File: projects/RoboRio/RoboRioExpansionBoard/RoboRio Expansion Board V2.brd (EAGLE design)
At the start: 56.6 x 77.5 mm, 125 parts, among them J1 RRINTERFACE-FEMALE, J10 SPI_MISO, J11 SPI_MOSI, J12 I2C_SCL, J13 I2C_SDA, J14 UART_TX, J15 UART_RX, J16 LCD, J17 ADC1, J18 ADC2, J19 ADC3, J2 MICROSD-HINGED, J20 ADC4, J21 ADC5, J22 ADC6, J23 ADC7, J25 PWM0, J26 PWM1, J27 PWM2, J28 PWM3, J29 PWM4, J3 51387-0578, J30 PWM5, J31 PWM6, J32 PWM7, J33 PWM8, J34 PWM9, J35 AI0, J36 AI1, J37 AI2, J38 AI3, J39 AO0, J4 GPIO0, J40 AO1, J5 GPIO1, J6 GPIO2, J7 GPIO3, J8 SPI_CS, J9 SPI_CLK, Q1 NPN-SOT416, Q2 NPN-SOT416, Q3 NPN-SOT416, U1 P8X32A-Q44_P, U2 24LC256ST, U3 FT232RL, U4 TC54VN43, U5 TPS2115APWR, U6 REG1117, U7 ADC124S01, U8 ADC124S01, Y1 5MHz

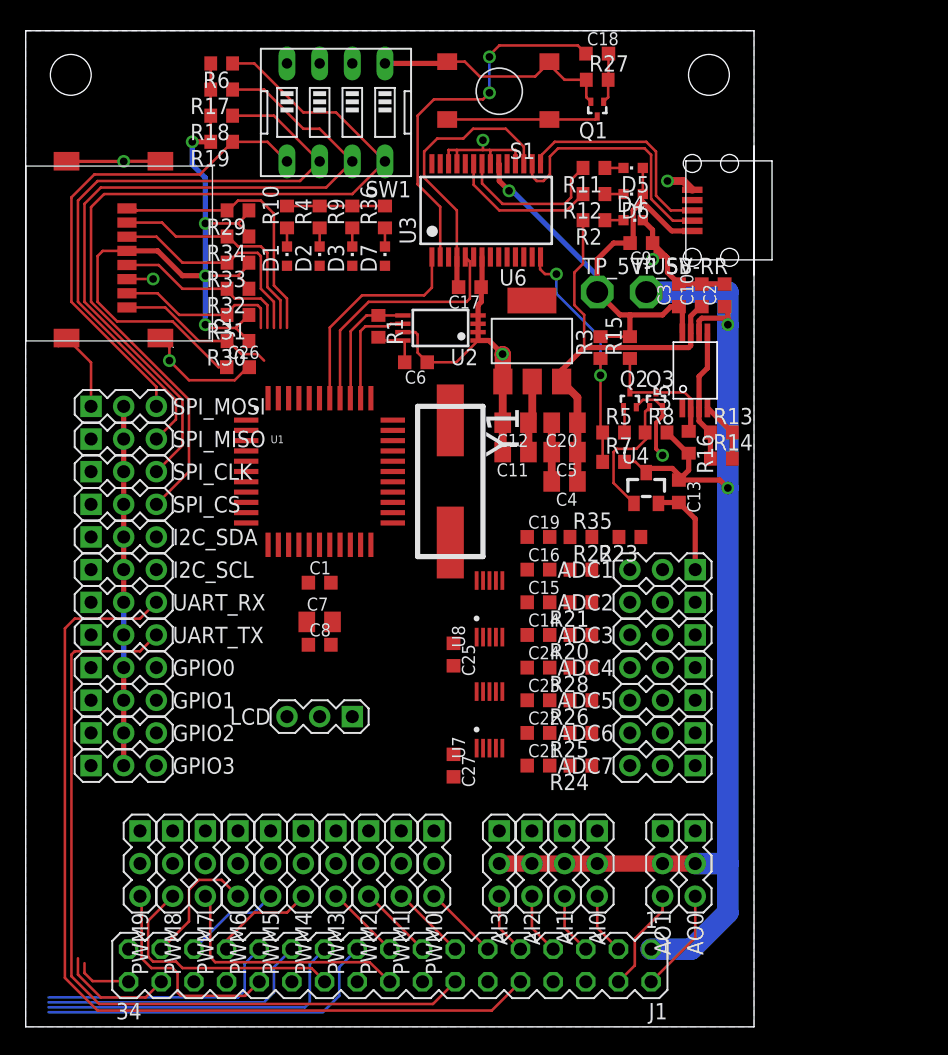
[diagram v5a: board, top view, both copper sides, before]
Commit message: Fixed ADC GND/DGND & VA/+3V3 issue
also lost of routing for the ADCs
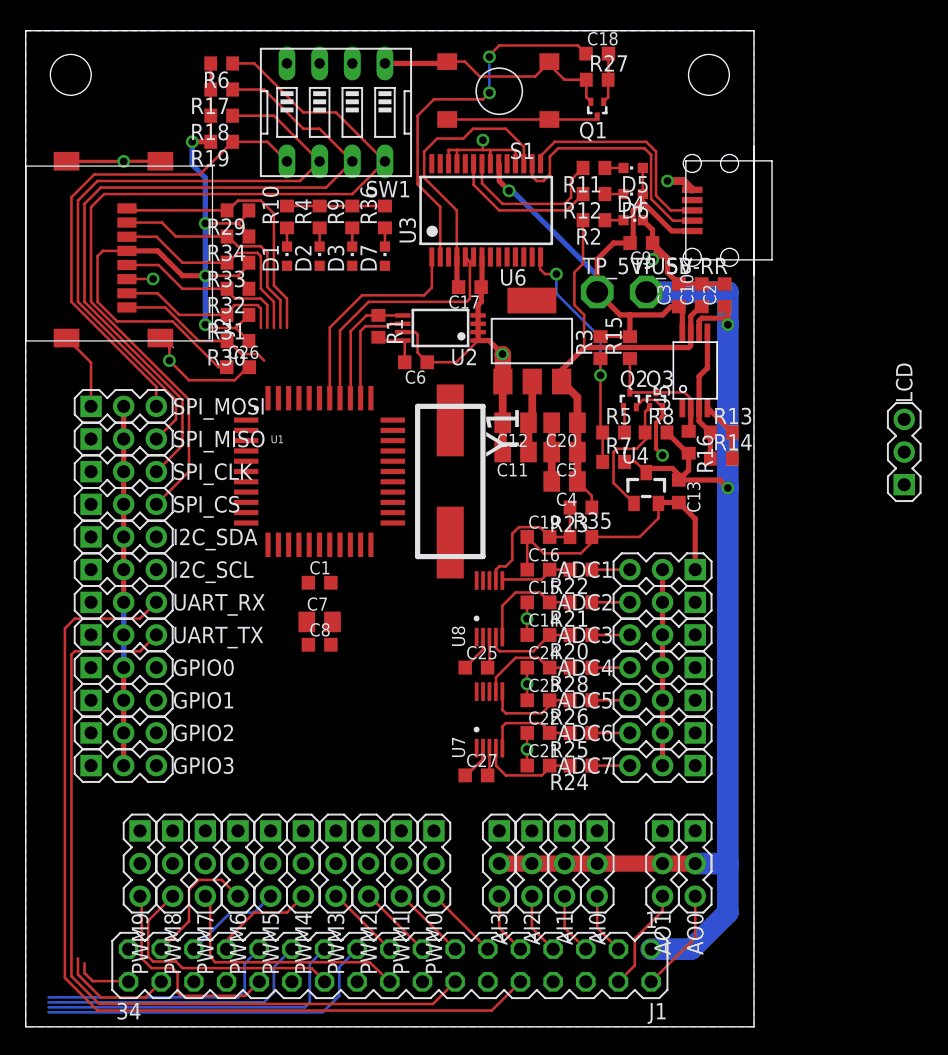
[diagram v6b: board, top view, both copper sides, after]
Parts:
- moved J16 49.9 mm to (68.3, 44.7), turned to 90 degrees
- moved R23 4.44 mm to (43.2, 40.4)
- moved C25 2.05 mm to (35.1, 27.9), turned to 0 degrees
- moved C27 1.93 mm to (35.1, 19.6), turned to 0 degrees
- turned R22 to 180 degrees
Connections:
- removed net GND: C25.2, C27.2, U7.P$3, U8.P$3
- removed net VA: C25.1, C27.1, U7.P$2, U8.P$2
- net +3V3: now also C25.1, C27.1, U7.P$2, U8.P$2
- net DGND: now also C25.2, C27.2, U7.P$3, U8.P$3
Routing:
- net DGND: track 130.8 -> 158.9 mm, vias 8 -> 11
- net +3V3: track 100.8 -> 121.6 mm
- net N$25: track 0.00 -> 11.8 mm
- net N$21: track 0.00 -> 8.44 mm
- net N$10: track 0.00 -> 7.83 mm
- net N$41: track 0.00 -> 7.81 mm
- net N$30: track 0.00 -> 7.45 mm
- net N$38: track 0.00 -> 7.45 mm
- net N$15: track 0.00 -> 7.24 mm
- net N$16: track 0.00 -> 5.70 mm
- net N$9: track 0.00 -> 2.96 mm
- net N$8: track 0.00 -> 2.96 mm
- net N$42: track 0.00 -> 2.96 mm
- net N$39: track 0.00 -> 2.96 mm
- net N$36: track 0.00 -> 2.96 mm
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
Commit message: routed I2C; other small fixes
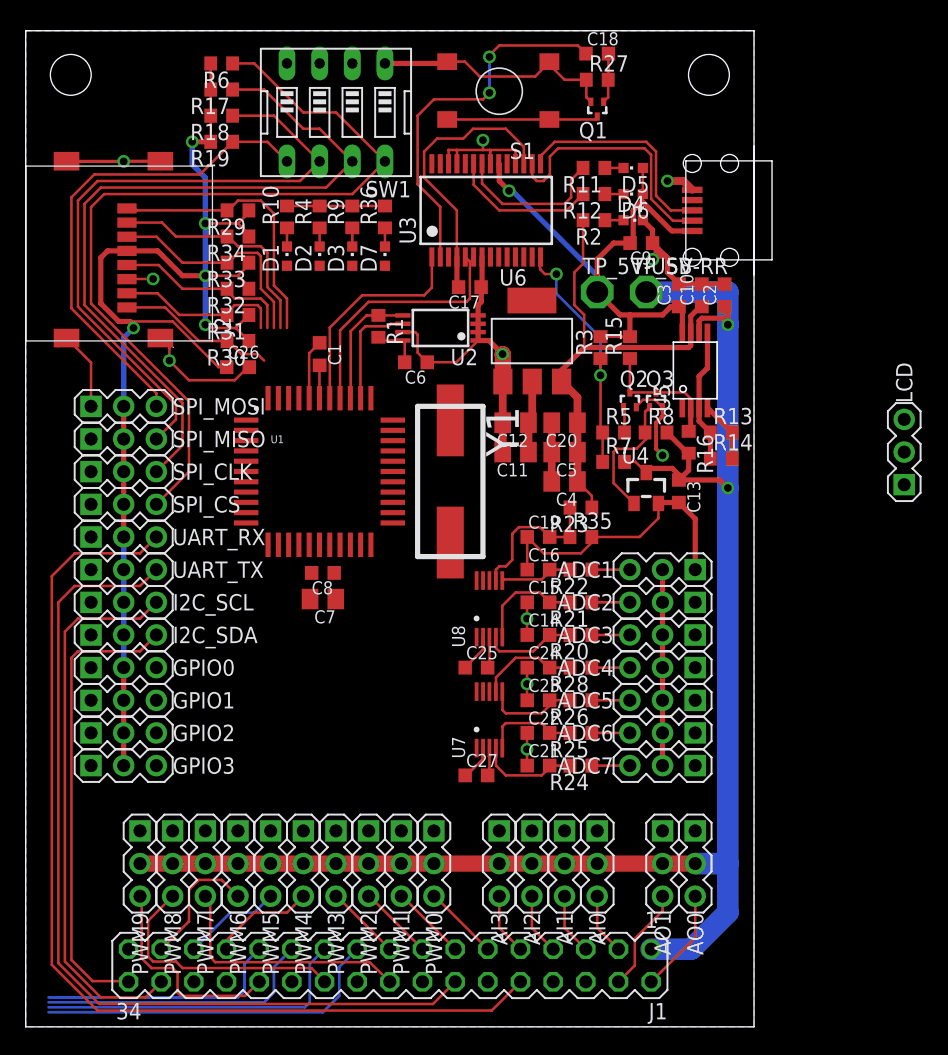
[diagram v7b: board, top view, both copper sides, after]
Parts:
- moved C1 17.8 mm to (22.9, 52.3), turned to 270 degrees
- moved J13 7.62 mm to (7.62, 30.5)
- moved C8 5.59 mm to (23.1, 35.3), turned to 180 degrees
- moved J14 5.08 mm to (7.62, 35.6)
- moved J15 5.08 mm to (7.62, 38.1)
- moved J12 2.54 mm to (7.62, 33.0)
- moved C7 1.80 mm to (23.1, 33.3), turned to 180 degrees
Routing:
- net IO13: track 8.99 -> 42.9 mm
- net IO14: track 4.48 -> 36.0 mm
- net 5VRR: track 98.5 -> 126.4 mm
- net +3V3: track 121.6 -> 132.8 mm, vias 4 -> 5
- net IO19: track 63.7 -> 69.6 mm
- net IO8: track 72.5 -> 78.5 mm
- net DGND: track 158.9 -> 161.6 mm

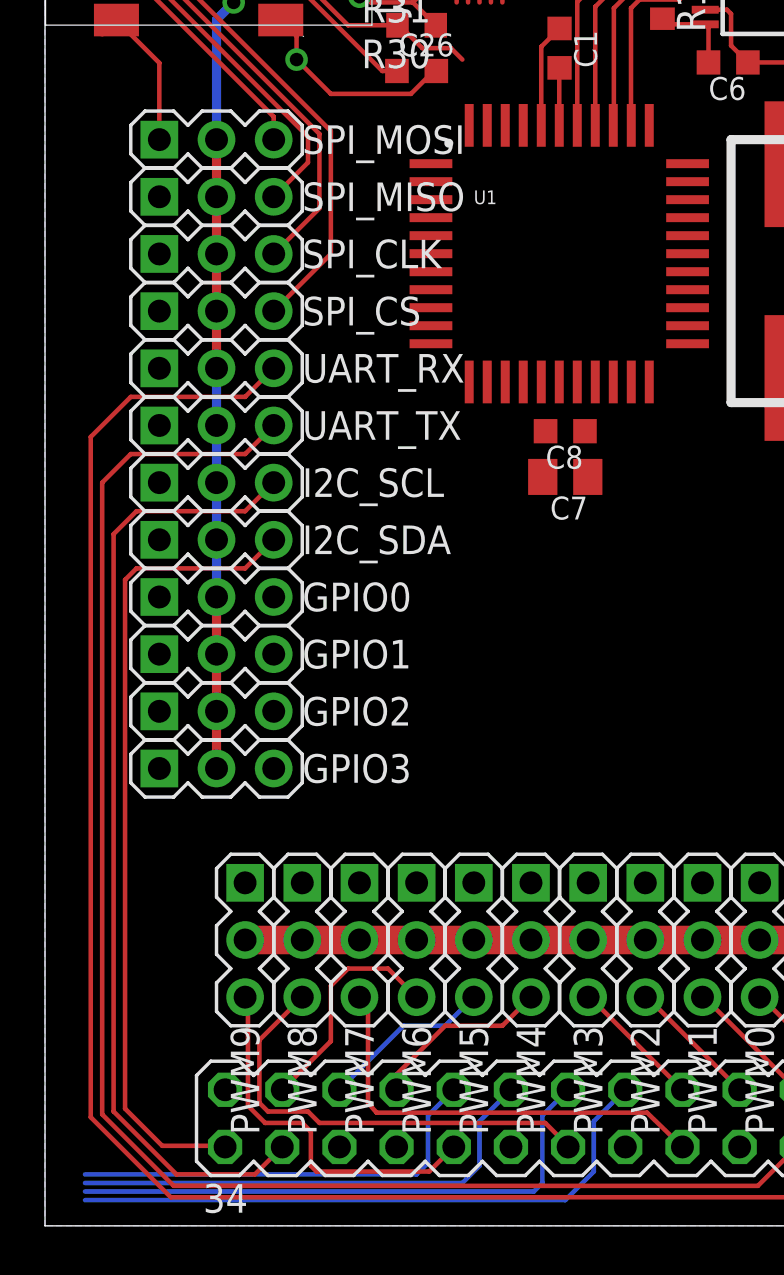
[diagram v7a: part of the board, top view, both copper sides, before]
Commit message: Routed SPI pins
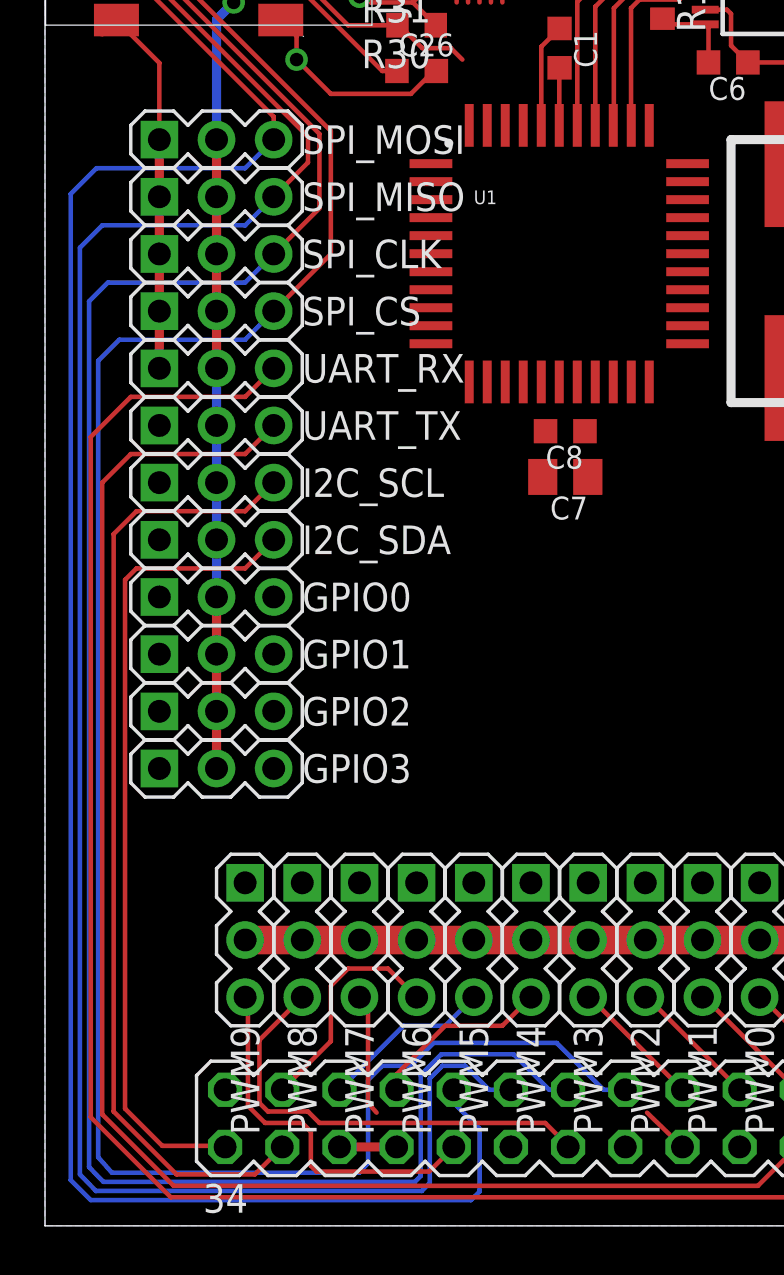
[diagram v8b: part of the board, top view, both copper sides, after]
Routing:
- net IO12: track 57.4 -> 115.7 mm
- net IO11: track 72.4 -> 126.3 mm
- net IO10: track 83.7 -> 133.4 mm
- net IO9: track 94.0 -> 139.9 mm
- net DGND: track 161.6 -> 174.3 mm
- net PWM7: track 19.6 -> 7.62 mm
